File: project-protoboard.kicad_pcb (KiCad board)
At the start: 2 copper layers, 50.8 x 81.3 mm, 68 parts, among them J1 SM04B-SRSS-TB(LF)(SN), J10 Conn_01x05_Socket, J11 Conn_01x05_Socket, J12 Conn_01x07_Socket, J13 Conn_01x07_Socket, J14 Conn_01x07_Socket, J15 Conn_01x07_Socket, J16 Conn_01x07_Socket, J17 Conn_01x07_Socket, J18 Conn_01x05_Socket, J19 Conn_01x05_Socket, J2 Conn_01x07_Socket, J20 Conn_01x05_Socket, J21 Conn_01x05_Socket, J22 Conn_01x07_Socket, J23 Conn_01x07_Socket, J24 Conn_01x07_Socket, J25 Conn_01x07_Socket, J26 Conn_01x07_Socket, J27 Conn_01x07_Socket, J28 Conn_01x07_Socket, J29 Conn_01x07_Socket, J3 Conn_01x07_Socket, J30 Conn_01x05_Socket, J31 Conn_01x05_Socket, J32 Conn_01x30_Socket, J33 Conn_01x30_Socket, J34 Conn_01x30_Socket, J35 Conn_01x07_Socket, J36 Conn_01x07_Socket, J37 Conn_01x07_Socket, J38 Conn_01x07_Socket, J39 Conn_01x07_Socket, J4 Conn_01x07_Socket, J40 Conn_01x07_Socket, J41 Conn_01x07_Socket, J42 Conn_01x07_Socket, J43 Conn_01x05_Socket, J44 Conn_01x05_Socket, J45 Conn_01x07_Socket, J46 Conn_01x07_Socket, J47 Conn_01x07_Socket, J48 Conn_01x07_Socket, J49 Conn_01x07_Socket, J5 Conn_01x07_Socket, J50 Conn_01x07_Socket, J51 Conn_01x07_Socket, J52 Conn_01x07_Socket, J53 Conn_01x07_Socket, J54 Conn_01x07_Socket, J55 Conn_01x07_Socket, J56 Conn_01x07_Socket, J57 Conn_01x07_Socket, J58 Conn_01x07_Socket, J59 Conn_01x07_Socket, J6 Conn_01x07_Socket, J60 Conn_01x07_Socket, J61 Conn_01x07_Socket, J62 Conn_01x07_Socket, J63 Conn_01x05_Socket, J64 Conn_01x05_Socket, J7 Conn_01x07_Socket, J8 Conn_01x07_Socket, J9 Conn_01x07_Socket

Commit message: First complete draft
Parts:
- removed the J37 at (104.1, 33.0)
- removed the J38 at (104.1, 35.6)
- added J32: Conn_01x06_Socket, Proto:Proto_1x06_P2.54mm, F.Cu at (81.3, 86.4)
- added J33: Conn_01x06_Socket, Proto:Proto_1x06_P2.54mm, F.Cu at (81.3, 88.9)
- added J65: Conn_01x06_Socket, Proto:Proto_1x06_P2.54mm, F.Cu at (101.6, 88.9)
- added J66: Conn_01x06_Socket, Proto:Proto_1x06_P2.54mm, F.Cu at (101.6, 91.4)
- added J67: Conn_01x06_Socket, Proto:Proto_1x06_P2.54mm, F.Cu at (101.6, 94.0)
- added J68: Conn_01x06_Socket, Proto:Proto_1x06_P2.54mm, F.Cu at (101.6, 96.5)
- added J69: Conn_01x26_Socket, Proto:Proto_1x26_P2.54mm, F.Cu at (119.4, 27.9)
- added J70: Conn_01x26_Socket, Proto:Proto_1x26_P2.54mm, F.Cu at (116.8, 27.9)
- added JP1: SolderJumper_2_Open, Jumper:SolderJumper-2_P1.3mm_Open_RoundedPad1.0x1.5mm, F.Cu at (80.7, 99.1)
- added JP2: SolderJumper_2_Open, Jumper:SolderJumper-2_P1.3mm_Open_RoundedPad1.0x1.5mm, F.Cu at (73.7, 92.1)
- added JP3: SolderJumper_2_Open, Jumper:SolderJumper-2_P1.3mm_Open_RoundedPad1.0x1.5mm, F.Cu at (95.9, 99.1)
- added JP4: SolderJumper_2_Open, Jumper:SolderJumper-2_P1.3mm_Open_RoundedPad1.0x1.5mm, F.Cu at (99.7, 99.1)
- added JP5: SolderJumper_2_Open, Jumper:SolderJumper-2_P1.3mm_Open_RoundedPad1.0x1.5mm, F.Cu at (121.9, 92.1)
- added JP6: SolderJumper_2_Open, Jumper:SolderJumper-2_P1.3mm_Open_RoundedPad1.0x1.5mm, F.Cu at (114.9, 99.1)
- J10, J11, J30, J31, J43, J44, J63, J64: value Conn_01x05_Socket -> Conn_01x06_Socket; footprint Proto:Proto_1x05_P2.54mm -> Proto:Proto_1x06_P2.54mm
- J12, J13, J14, J15, J16, J17, J22, J23, J24, J25, J26, J27, J28, J29, J35, J36, J39, J40, J41, J42, J45, J46, J47, J48, J49, J50, J51, J52, J53, J54, J55, J56, J57, J58, J59, J60, J61, J62, J7, J8, J9: value Conn_01x07_Socket -> Conn_01x06_Socket; footprint Proto:Proto_1x07_P2.54mm -> Proto:Proto_1x06_P2.54mm
- J2: value Conn_01x07_Socket -> Conn_01x04_Socket; footprint Proto:Proto_1x07_P2.54mm -> Proto:Proto_1x04_P2.54mm
- J3, J5: value Conn_01x07_Socket -> Conn_01x09_Socket; footprint Proto:Proto_1x07_P2.54mm -> Proto:Proto_1x09_P2.54mm
- J34: value Conn_01x30_Socket -> Conn_01x06_Socket; footprint Proto:Proto_1x30_P2.54mm -> Proto:Proto_1x06_P2.54mm
- J4, J6: value Conn_01x07_Socket -> Conn_01x13_Socket; footprint Proto:Proto_1x07_P2.54mm -> Proto:Proto_1x13_P2.54mm
- moved J35 69.9 mm to (81.3, 94.0)
- moved J36 69.9 mm to (81.3, 96.5)
- moved J4 28.1 mm to (78.7, 61.0), turned to 180 degrees
- moved J15 23.4 mm to (81.3, 43.2)
- moved J17 23.4 mm to (81.3, 48.3)
- moved J14 23.4 mm to (81.3, 40.6)
- moved J16 23.4 mm to (81.3, 45.7)
- moved J2 23.4 mm to (81.3, 50.8), turned to 180 degrees
- moved J6 22.9 mm to (76.2, 61.0), turned to 180 degrees
- moved J34 19.7 mm to (81.3, 91.4), turned to -90 degrees
- moved J7 18.5 mm to (81.3, 22.9)
- moved J8 18.5 mm to (81.3, 25.4)
- moved J9 18.5 mm to (81.3, 27.9)
- moved J39 15.5 mm to (101.6, 22.9)
- moved J40 15.5 mm to (101.6, 25.4)
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- renumbered J32 to J37, J33 to J38
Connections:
- net VCC renamed Net-(J37-Pin_1)
- J1 pad 2: VDD -> /VDD
- J2 pad 1: Net-(J2-Pin_1) -> GND
- J2 pad 2: Net-(J2-Pin_1) -> /VDD
- J2 pad 3: Net-(J2-Pin_1) -> /SCA
- J2 pad 4: Net-(J2-Pin_1) -> /SCL
- J34 pad 1: VDD -> Net-(J34-Pin_1)
- J34 pad 2: VDD -> Net-(J34-Pin_1)
- J34 pad 3: VDD -> Net-(J34-Pin_1)
- J34 pad 4: VDD -> Net-(J34-Pin_1)
- J34 pad 5: VDD -> Net-(J34-Pin_1)
- J34 pad 6: VDD -> Net-(J34-Pin_1)
- J38 pad 1: GND -> Net-(J38-Pin_1)
- J38 pad 10: GND -> Net-(J38-Pin_1)
- J38 pad 11: GND -> Net-(J38-Pin_1)
- J38 pad 12: GND -> Net-(J38-Pin_1)
- J38 pad 13: GND -> Net-(J38-Pin_1)
- J38 pad 14: GND -> Net-(J38-Pin_1)
- J38 pad 15: GND -> Net-(J38-Pin_1)
- J38 pad 16: GND -> Net-(J38-Pin_1)
- J38 pad 17: GND -> Net-(J38-Pin_1)
- J38 pad 18: GND -> Net-(J38-Pin_1)
- J38 pad 19: GND -> Net-(J38-Pin_1)
- J38 pad 2: GND -> Net-(J38-Pin_1)
- J38 pad 20: GND -> Net-(J38-Pin_1)
- J38 pad 21: GND -> Net-(J38-Pin_1)
- J38 pad 22: GND -> Net-(J38-Pin_1)
- J38 pad 23: GND -> Net-(J38-Pin_1)
- J38 pad 24: GND -> Net-(J38-Pin_1)
- J38 pad 25: GND -> Net-(J38-Pin_1)
- J38 pad 26: GND -> Net-(J38-Pin_1)
- J38 pad 27: GND -> Net-(J38-Pin_1)
- J38 pad 28: GND -> Net-(J38-Pin_1)
- J38 pad 29: GND -> Net-(J38-Pin_1)
- J38 pad 3: GND -> Net-(J38-Pin_1)
- J38 pad 30: GND -> Net-(J38-Pin_1)
- J38 pad 4: GND -> Net-(J38-Pin_1)
- J38 pad 5: GND -> Net-(J38-Pin_1)
- J38 pad 6: GND -> Net-(J38-Pin_1)
- J38 pad 7: GND -> Net-(J38-Pin_1)
- J38 pad 8: GND -> Net-(J38-Pin_1)
- J38 pad 9: GND -> Net-(J38-Pin_1)
- J4 pad 1: Net-(J4-Pin_1) -> Net-(J3-Pin_1)
- J4 pad 2: Net-(J4-Pin_1) -> Net-(J3-Pin_1)
- J4 pad 3: Net-(J4-Pin_1) -> Net-(J3-Pin_1)
- J4 pad 4: Net-(J4-Pin_1) -> Net-(J3-Pin_1)
- J4 pad 5: Net-(J4-Pin_1) -> Net-(J3-Pin_1)
- J4 pad 6: Net-(J4-Pin_1) -> Net-(J3-Pin_1)
- J4 pad 7: Net-(J4-Pin_1) -> Net-(J3-Pin_1)
- J6 pad 1: Net-(J6-Pin_1) -> Net-(J5-Pin_1)
- J6 pad 2: Net-(J6-Pin_1) -> Net-(J5-Pin_1)
- J6 pad 3: Net-(J6-Pin_1) -> Net-(J5-Pin_1)
- J6 pad 4: Net-(J6-Pin_1) -> Net-(J5-Pin_1)
- J6 pad 5: Net-(J6-Pin_1) -> Net-(J5-Pin_1)
- J6 pad 6: Net-(J6-Pin_1) -> Net-(J5-Pin_1)
- J6 pad 7: Net-(J6-Pin_1) -> Net-(J5-Pin_1)
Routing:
- net Net-(J38-Pin_1): track 0.00 -> 81.3 mm
- net Net-(J37-Pin_1): track 0.00 -> 76.2 mm
- net Net-(J3-Pin_1): track 0.00 -> 73.8 mm
- net Net-(J70-Pin_1): track 0.00 -> 71.6 mm
- net Net-(J5-Pin_1): track 0.00 -> 68.4 mm
- net Net-(J69-Pin_1): track 0.00 -> 66.1 mm
- net GND: track 0.00 -> 15.4 mm, vias 0 -> 8
- net Net-(J39-Pin_1): track 0.00 -> 15.2 mm
- net Net-(J9-Pin_1): track 0.00 -> 12.7 mm
- net Net-(J8-Pin_1): track 0.00 -> 12.7 mm
- net Net-(J7-Pin_1): track 0.00 -> 12.7 mm
- net Net-(J68-Pin_1): track 0.00 -> 12.7 mm
- net Net-(J67-Pin_1): track 0.00 -> 12.7 mm
- net Net-(J66-Pin_1): track 0.00 -> 12.7 mm
- net Net-(J65-Pin_1): track 0.00 -> 12.7 mm
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- added copper zone on B.Cu, net GND
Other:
- outline, holes or cut-outs redrawn
- board text added: "+"
- board text added: "A"
- board text added: "Connect to"
- board text added: "GND"
- board text added: "SCL"
- board text added: "backplane"

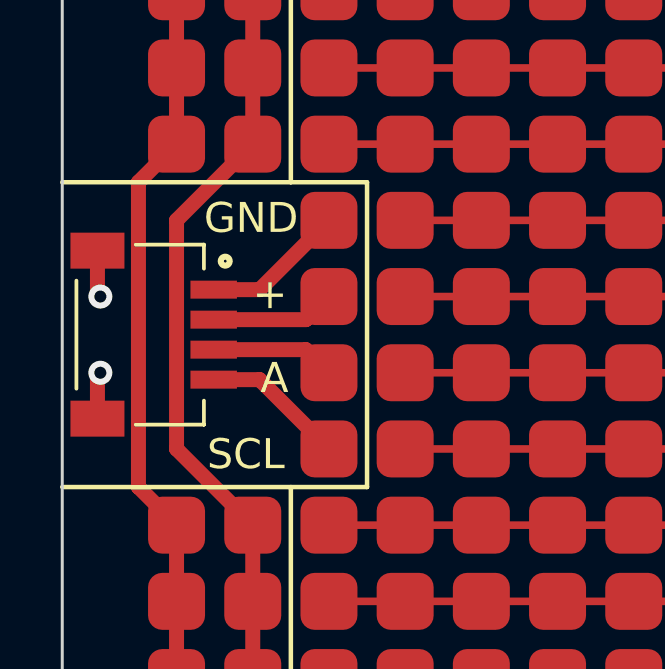
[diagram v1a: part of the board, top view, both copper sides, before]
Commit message: Add forgotten connection to ground
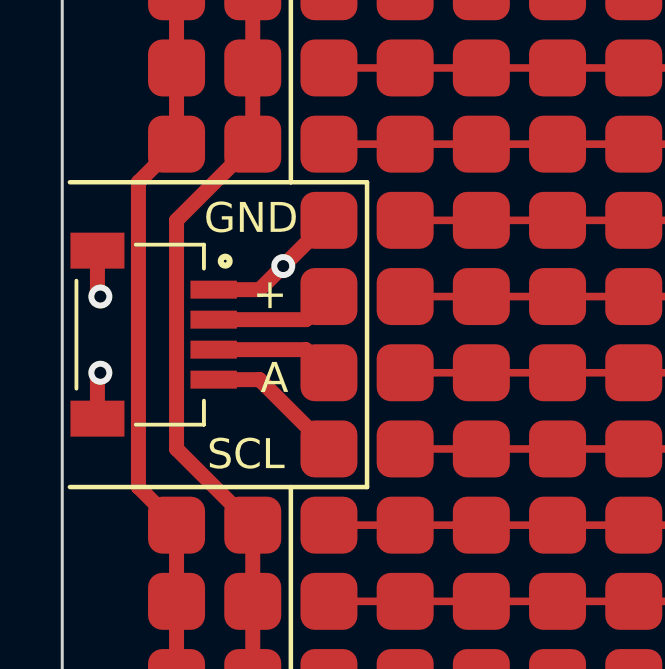
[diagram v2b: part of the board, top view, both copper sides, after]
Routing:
- net GND: vias 8 -> 9
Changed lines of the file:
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@@
   (gr_line (start 95.25 97.79) (end 95.25 21.59)
     (stroke (width 0.15) (type default)) (layer "F.SilkS"))
-  (gr_line (start 82.55 59.69) (end 72.39 59.69)
+  (gr_line (start 82.55 59.69) (end 72.644 59.69)
     (stroke (width 0.15) (type default)) (layer "F.SilkS"))
-  (gr_line (start 72.39 49.53) (end 82.55 49.53)
+  (gr_line (start 72.644 49.53) (end 82.55 49.53)
     (stroke (width 0.15) (type default)) (layer "F.SilkS"))
   (gr_line (start 100.33 21.59) (end 100.33 97.79)
@@
   (segment (start 81.31 99.06) (end 82.55 99.06) (width 0.5) (layer "F.Cu") (net 1))
   (segment (start 73.563 55.977) (end 73.66 55.88) (width 0.5) (layer "F.Cu") (net 1))
-  (segment (start 78.97 53.11) (end 81.28 50.8) (width 0.5) (layer "F.Cu") (net 1))
+  (segment (start 78.97 53.11) (end 79.756 52.324) (width 0.5) (layer "F.Cu") (net 1))
   (segment (start 100.36 99.06) (end 101.6 99.06) (width 0.5) (layer "F.Cu") (net 1))
   (segment (start 95.22 99.06) (end 93.98 99.06) (width 0.5) (layer "F.Cu") (net 1))
@@
   (segment (start 73.563 57.41) (end 73.563 55.977) (width 0.5) (layer "F.Cu") (net 1))
   (segment (start 77.438 53.11) (end 78.97 53.11) (width 0.5) (layer "F.Cu") (net 1))
+  (segment (start 79.756 52.324) (end 81.28 50.8) (width 0.5) (layer "F.Cu") (net 1))
   (segment (start 73.563 51.81) (end 73.563 53.243) (width 0.5) (layer "F.Cu") (net 1))
   (via (at 73.66 55.88) (size 0.8) (drill 0.4) (layers "F.Cu" "B.Cu") (net 1))
@@
   (via (at 121.92 93.98) (size 0.8) (drill 0.4) (layers "F.Cu" "B.Cu") (net 1))
   (via (at 101.6 99.06) (size 0.8) (drill 0.4) (layers "F.Cu" "B.Cu") (net 1))
+  (via (at 79.756 52.324) (size 0.8) (drill 0.4) (layers "F.Cu" "B.Cu") (net 1))
   (via (at 93.98 99.06) (size 0.8) (drill 0.4) (layers "F.Cu" "B.Cu") (net 1))
   (segment (start 80.51 55.11) (end 81.28 55.88) (width 0.5) (layer "F.Cu") (net 2))
